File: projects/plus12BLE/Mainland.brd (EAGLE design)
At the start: 114.3 x 80 mm, 71 parts, among them J1 USB-CWM2.0, SW1 RSTSWSMD, SW2 RSTSWSMD, U1 BL652-SA-01-T/R, U2 MCP73831T-2ACI/OT, U4 CP2102N-A01-GQFN20

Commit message: working for DFM, new USB connector test
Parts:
- removed JP2: (no value), pinhead:1X04
- removed JP3: (no value), pinhead:1X05/90
- added J2: RA 6Pin SMD, SparkFun-Connectors:1X04_SMD_RA_FEMALE
- added J3: RA 6Pin SMD, SparkFun-Connectors:1X06-SMD_RA_MALE
- added SW3: SLIDER_SWITCH, Keys:MHSS1105
- added U$4: (no value), Logos:IEEE_BERKELEY
- C4, C6: device resistor:C0402K -> resistor:C0603
- R1, R10, R2, R3, R4, R5, R6, R7, R8, R9: device resistor:R0402 -> resistor:R0603
- SW1, SW2: value RSTSWSMD -> RSTSWSMALL_SMD; device Keys:FLATSWT -> Keys:EVP-BBA
- U$2: device Logos:1INCH_BOT -> Logos:BAC_SELLOUT
- U$3: value SLIDER_SWITCH -> (none); device Keys:MHSS1105 -> Logos:1INCH_TOP
- moved FRAME2 245.7 mm to (64.8, 121.9)
- moved U$3 206.0 mm to (76.2, 71.1), flipped to the bottom
- moved U$2 72.2 mm to (122.6, 61.0), flipped to the bottom
- moved SW1 46.8 mm to (117.5, 80.0), turned to 270 degrees
- moved SW2 42.2 mm to (117.5, 76.2), turned to 90 degrees
- moved R3 30.2 mm to (100.3, 114.3), turned to 180 degrees
- moved C2 26.7 mm to (104.8, 116.8)
- moved U2 26.7 mm to (101.0, 116.8)
- moved R2 15.9 mm to (95.9, 118.7), turned to 0 degrees
- moved C4 7.62 mm to (84.5, 118.7)
- moved R5 7.62 mm to (81.3, 118.7)
- moved R6 7.62 mm to (87.6, 118.7)
- moved LED1 6.98 mm to (92.1, 118.7), turned to 270 degrees
- moved R4 5.71 mm to (57.8, 117.5)
- moved FRAME1 4.96 mm to (50.2, 124.5)
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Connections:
- net 3.3V: now also J2.4; no longer JP2.1, JP3.1
- net DFU: now also SW2.A1, SW2.A2; no longer SW2.P$1, SW2.P$2, SW2.P$5, SW2.P$6
- net GND: now also J2.1, J3.1, SW1.B1, SW1.B2, SW2.B1, SW2.B2; no longer JP2.4, JP3.5, SW1.P$3, SW1.P$4, SW1.P$7, SW1.P$8, SW2.P$3, SW2.P$4, SW2.P$7, SW2.P$8
- net N$21: now also SW3.COMM; no longer U$3.COMM
- net N$27: now also SW3.1; no longer U$3.1
- net RESET: now also SW1.A1, SW1.A2; no longer SW1.P$1, SW1.P$2, SW1.P$5, SW1.P$6
- net RX0: now also J3.5; no longer JP3.2
- net SWDCLK: now also J2.2; no longer JP2.3
- net SWDIO: now also J2.3; no longer JP2.2
- net TX0: now also J3.4; no longer JP3.3
- net V_USB: now also J3.3; no longer JP3.4
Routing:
- net ROW1: track 0.00 -> 181.8 mm
- net ROW2: track 0.00 -> 133.3 mm
- net ROW3: track 0.00 -> 118.1 mm
- net V_BATT: track 2.76 -> 119.4 mm
- net COL1: track 0.00 -> 111.4 mm
- net COL6: track 0.00 -> 109.8 mm, vias 0 -> 1
- net V_USB: track 6.07 -> 90.1 mm, vias 1 -> 4
- net COL2: track 0.00 -> 83.6 mm
- net COL5: track 0.00 -> 83.6 mm
- net COL3: track 0.00 -> 83.6 mm
- net COL4: track 0.00 -> 83.6 mm
- net BATT_M: track 5.55 -> 50.8 mm, vias 0 -> 2
- net N$18: track 0.00 -> 30.3 mm
- net N$13: track 0.00 -> 22.3 mm
- net N$8: track 0.00 -> 21.2 mm
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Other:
- board text added: "GND"
- board text added: "SWD 3v3"
- board text added: "UART HEADER"

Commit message: saving before autorouter
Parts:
- J1: value USB-CWM2.0 -> USB-C2.0WM2.0
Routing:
- net N$20: track 19.0 -> 12.7 mm
- net DMINUS: track 3.59 -> 9.05 mm, vias 2 -> 1
- net GND: track 36.5 -> 33.6 mm
- net V_USB: track 90.1 -> 92.1 mm, vias 4 -> 6

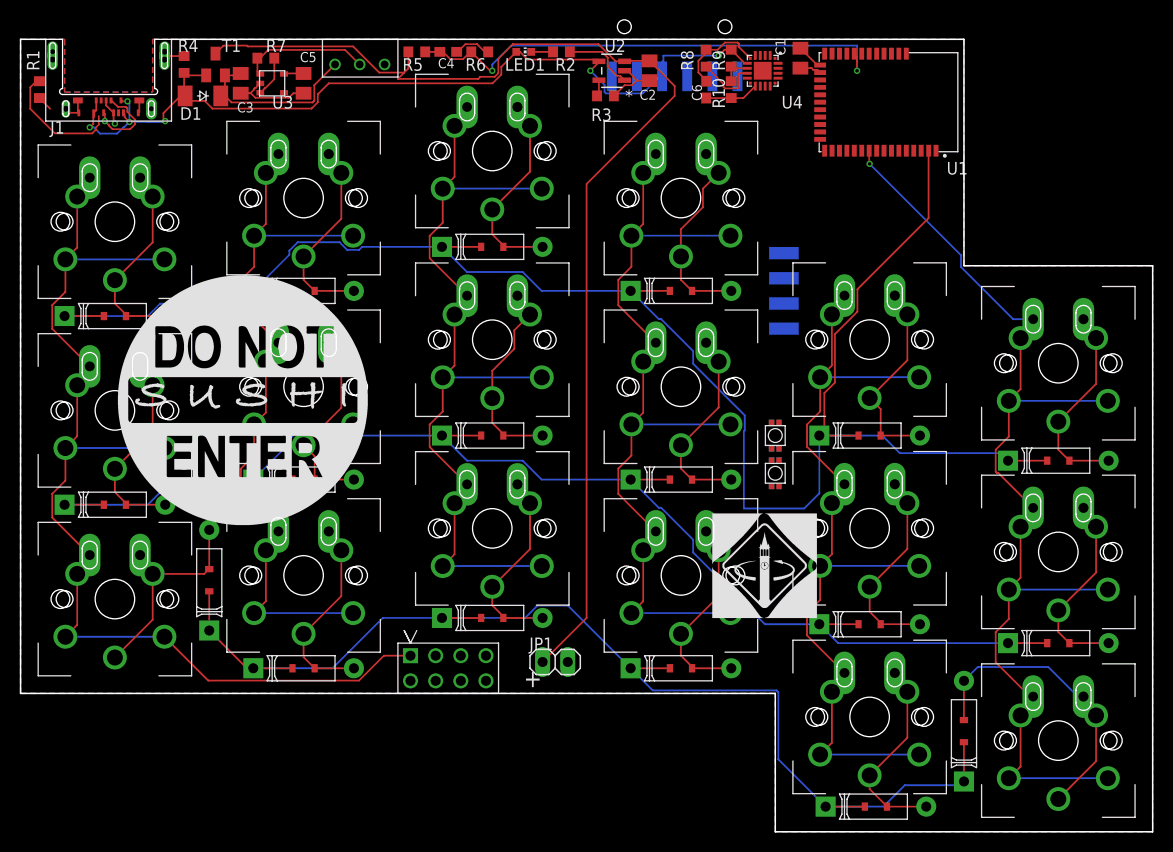
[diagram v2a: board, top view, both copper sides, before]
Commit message: revB of plus12BLE and necessary library changes
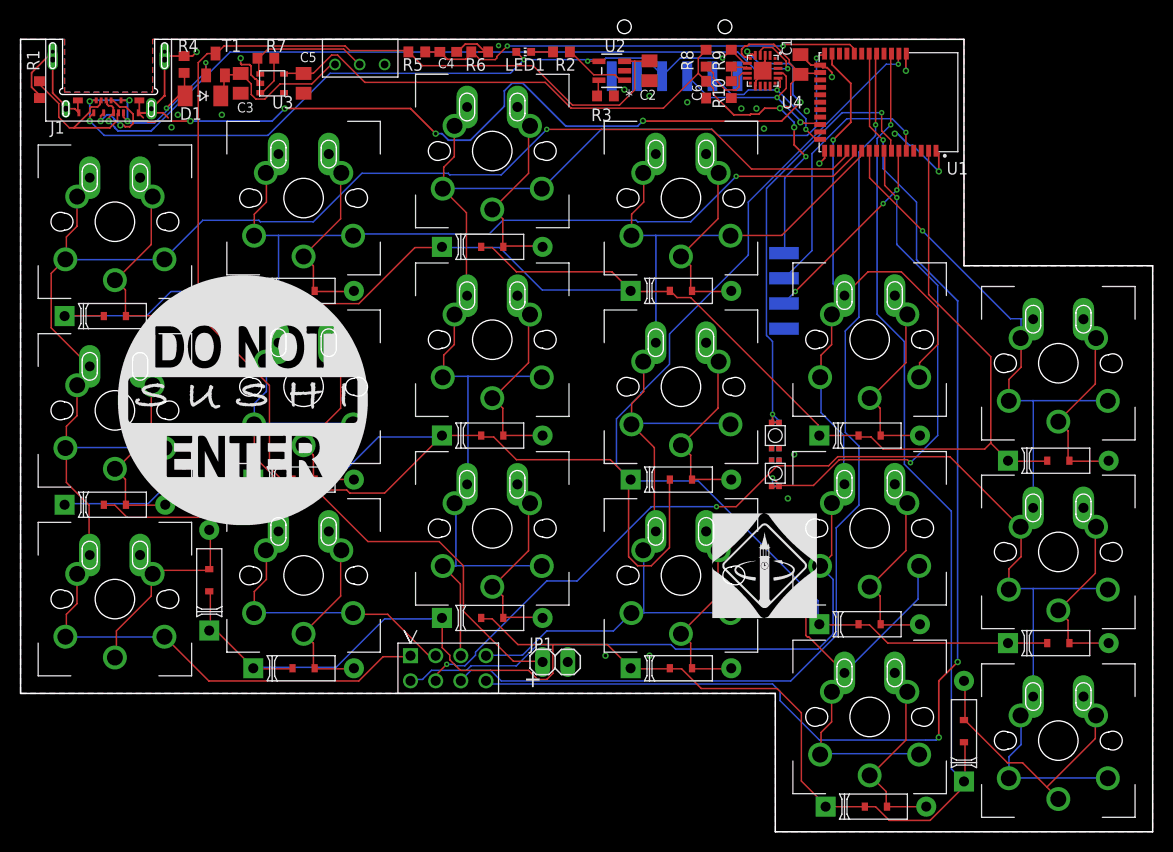
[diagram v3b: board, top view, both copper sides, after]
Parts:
- moved FRAME2 62.8 mm to (46.0, 62.0), turned to 90 degrees
- moved C1 0.64 mm to (120.0, 117.5)
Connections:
- net DFU: now also SW2.A3, SW2.A4
- net GND: now also SW1.B3, SW1.B4, SW2.B3, SW2.B4
- net RESET: now also SW1.A3, SW1.A4
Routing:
- net ROW6T2: track 0.00 -> 122.4 mm, vias 0 -> 3
- net ROW5T1: track 0.00 -> 102.3 mm, vias 0 -> 1
- net COL5: track 83.6 -> 175.5 mm, vias 0 -> 1
- net ROW2: track 133.3 -> 223.8 mm, vias 0 -> 1
- net DMINUS: track 9.05 -> 94.5 mm, vias 1 -> 8
- net ROW3: track 118.1 -> 199.3 mm, vias 0 -> 1
- net 3.3V: track 13.6 -> 92.3 mm, vias 0 -> 3
- net DPLUS: track 2.71 -> 80.5 mm, vias 1 -> 2
- net COL1: track 111.4 -> 187.9 mm, vias 0 -> 1
- net COL6: track 109.8 -> 176.9 mm, vias 1 -> 3
- net COL2: track 83.6 -> 145.4 mm, vias 0 -> 1
- net DFU: track 0.00 -> 52.9 mm, vias 0 -> 3
- net RESET: track 0.00 -> 46.6 mm, vias 0 -> 2
- net COL3: track 83.6 -> 128.9 mm, vias 0 -> 1
- net COL4: track 83.6 -> 113.9 mm
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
